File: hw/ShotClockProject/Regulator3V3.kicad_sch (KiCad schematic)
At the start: 11 parts, among them U2 TPS63000

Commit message: Finished rough layout of PCB (ready for review)
Changed battery polarity to match the batteries I have.
Added power led to voltage regulator
Removed old comments from schematic
Gave all footprints a 3D model
Replaced batttery footprint with a SMD JST 3 pins horizontal connector
Finished rough placement of components
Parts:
- added D2: G_LED, LED_SMD:LED_0603_1608Metric, symbol Device:LED
- added R10: 1k5, Resistor_SMD:R_0402_1005Metric, symbol Device:R
- U2: footprint Package_SON:Texas_DRC0010J_ThermalVias -> Package_SON_Altered:Texas_DRC0010J_ThermalVias_Altered
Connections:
- net 3v3_out: now also D2.1 (K), R10.1; no longer C16.1, C17.1, C18.1, R11.1, U2.1 (VOUT)
- net GND: now also R10.2
- new net: C16.1, C17.1, C18.1, D2.2 (A), R11.1, U2.1 (VOUT)
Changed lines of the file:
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@@
   (junction (at 83.82 67.31) (diameter 0) (color 0 0 0 0)
   )
+  (junction (at 139.7 38.1) (diameter 0) (color 0 0 0 0)
+  )
   (junction (at 139.7 48.26) (diameter 0) (color 0 0 0 0)
   )
-  (junction (at 139.7 38.1) (diameter 0) (color 0 0 0 0)
-  )
   (junction (at 59.69 38.1) (diameter 0) (color 0 0 0 0)
   )
   (junction (at 68.58 43.18) (diameter 0) (color 0 0 0 0)
   )
+  (junction (at 156.21 38.1) (diameter 0) (color 0 0 0 0)
+  )
   (junction (at 66.04 45.72) (diameter 0) (color 0 0 0 0)
   )
@@
     (stroke (width 0) (type default))
   )
+  (wire (pts (xy 139.7 38.1) (xy 139.7 40.64))
+    (stroke (width 0) (type default))
+  )
   (wire (pts (xy 139.7 48.26) (xy 134.62 48.26))
     (stroke (width 0) (type default))
@@
     (stroke (width 0) (type default))
   )
-  (wire (pts (xy 139.7 38.1) (xy 149.86 38.1))
-    (stroke (width 0) (type default))
-  )
   (wire (pts (xy 76.2 43.18) (xy 68.58 43.18))
     (stroke (width 0) (type default))
@@
     (stroke (width 0) (type default))
   )
+  (wire (pts (xy 154.94 38.1) (xy 156.21 38.1))
+    (stroke (width 0) (type default))
+  )
   (wire (pts (xy 102.87 45.72) (xy 96.52 45.72))
     (stroke (width 0) (type default))
@@
     (stroke (width 0) (type default))
   )
-  (wire (pts (xy 139.7 38.1) (xy 113.03 38.1))
+  (wire (pts (xy 156.21 38.1) (xy 156.21 43.18))
+    (stroke (width 0) (type default))
+  )
+  (wire (pts (xy 113.03 38.1) (xy 139.7 38.1))
     (stroke (width 0) (type default))
   )
@@
     (stroke (width 0) (type default))
   )
+  (wire (pts (xy 139.7 38.1) (xy 147.32 38.1))
+    (stroke (width 0) (type default))
+  )
   (wire (pts (xy 59.69 38.1) (xy 53.34 38.1))
     (stroke (width 0) (type default))
@@
     (stroke (width 0) (type default))
   )
+  (wire (pts (xy 156.21 50.8) (xy 156.21 53.34))
+    (stroke (width 0) (type default))
+  )
   (wire (pts (xy 73.66 48.26) (xy 73.66 49.53))
     (stroke (width 0) (type default))
@@
     (stroke (width 0) (type default))
   )
-  (wire (pts (xy 139.7 38.1) (xy 139.7 40.64))
+  (wire (pts (xy 156.21 38.1) (xy 157.48 38.1))
     (stroke (width 0) (type default))
   )
@@
     (effects (font (size 2.5 2.5) (color 255 0 0 1)) (justify left bottom))
   )
-  (hierarchical_label "3v3_out" (shape output) (at 149.86 38.1 0) (fields_autoplaced)
+  (hierarchical_label "3v3_out" (shape output) (at 157.48 38.1 0) (fields_autoplaced)
     (effects (font (size 1.27 1.27)) (justify left))
   )
   (hierarchical_label "batt_in" (shape input) (at 31.75 38.1 180) (fields_autoplaced)
     (effects (font (size 1.27 1.27)) (justify right))
+  )
+  (symbol (lib_id "Device:R") (at 156.21 46.99 0) (mirror y) (unit 1)
+    (in_bom yes) (on_board yes) (dnp no)
+    (property "Reference" "R10" (at 158.75 45.72 0)
+      (effects (font (size 1.27 1.27)) (justify right))
+    )
+    (property "Value" "1k5" (at 158.75 48.26 0)
+      (effects (font (size 1.27 1.27)) (justify right))
+    )
+    (property "Footprint" "Resistor_SMD:R_0402_1005Metric" (at 157.988 46.99 90)
+      (effects (font (size 1.27 1.27)) hide)
+    )
+    (property "Datasheet" "~" (at 156.21 46.99 0)
+      (effects (font (size 1.27 1.27)) hide)
+    )
+    (pin "1")
+    (pin "2")
+    (instances
+      (project "ShotClockProject"
+        (path "/5fd859aa-754d-49c2-9762-3f7ebe3bb64c"
+          (reference "R10") (unit 1)
+        )
+        (path "/5fd859aa-754d-49c2-9762-3f7ebe3bb64c/17367eb9-0f4d-4017-b1ca-d50430410a5d"
+          (reference "R28") (unit 1)
+        )
+      )
+    )
+  )
+  (symbol (lib_id "power:GND") (at 156.21 53.34 0) (mirror y) (unit 1)
+    (in_bom yes) (on_board yes) (dnp no) (fields_autoplaced)
+    (property "Reference" "#PWR033" (at 156.21 59.69 0)
+      (effects (font (size 1.27 1.27)) hide)
+    )
+    (property "Value" "GND" (at 156.21 58.42 0)
+      (effects (font (size 1.27 1.27)) hide)
+    )
+    (property "Footprint" "" (at 156.21 53.34 0)
+      (effects (font (size 1.27 1.27)) hide)
+    )
+    (property "Datasheet" "" (at 156.21 53.34 0)
+      (effects (font (size 1.27 1.27)) hide)
+    )
+    (pin "1")
+    (instances
+      (project "ShotClockProject"
+        (path "/5fd859aa-754d-49c2-9762-3f7ebe3bb64c"
+          (reference "#PWR033") (unit 1)
+        )
+        (path "/5fd859aa-754d-49c2-9762-3f7ebe3bb64c/17367eb9-0f4d-4017-b1ca-d50430410a5d"
+          (reference "#PWR074") (unit 1)
+        )
+      )
+    )
   )
   (symbol (lib_id "Device:C") (at 144.78 44.45 0) (mirror y) (unit 1)
@@
       (effects (font (size 1.27 1.27)))
     )
-    (property "Footprint" "Package_SON:Texas_DRC0010J_ThermalVias" (at 107.95 62.23 0)
+    (property "Footprint" "Package_SON_Altered:Texas_DRC0010J_ThermalVias_Altered" (at 107.95 62.23 0)
       (effects (font (size 1.27 1.27)) hide)
     )
@@
         )
       )
+    )
+  )
+  (symbol (lib_id "Device:LED") (at 151.13 38.1 0) (mirror y) (unit 1)
+    (in_bom yes) (on_board yes) (dnp no)
+    (property "Reference" "D2" (at 152.4 33.02 0)
+      (effects (font (size 1.27 1.27)) (justify right))
+    )
+    (property "Value" "G_LED" (at 149.86 35.56 0)
+      (effects (font (size 1.27 1.27)) (justify right))
+    )
+    (property "Footprint" "LED_SMD:LED_0603_1608Metric" (at 151.13 38.1 0)
+      (effects (font (size 1.27 1.27)) hide)
+    )
+    (property "Datasheet" "~" (at 151.13 38.1 0)
+      (effects (font (size 1.27 1.27)) hide)
+    )
+    (pin "1")
+    (pin "2")
+    (instances
+      (project "ShotClockProject"
+        (path "/5fd859aa-754d-49c2-9762-3f7ebe3bb64c"
+          (reference "D2") (unit 1)
+        )
+        (path "/5fd859aa-754d-49c2-9762-3f7ebe3bb64c/d287d155-1951-4d4f-8d6c-570f03bc79f5"
+          (reference "D3") (unit 1)
+        )
+        (path "/5fd859aa-754d-49c2-9762-3f7ebe3bb64c/17367eb9-0f4d-4017-b1ca-d50430410a5d"
+          (reference "D5") (unit 1)
+        )
+      )

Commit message: First feedback round from Luc on schematic
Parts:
- L1: value L -> 2.2uH
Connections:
- net 3v3_out: now also C16.1, C17.1, C18.1, D2.2 (A), R11.1, U2.1 (VOUT); no longer D2.1 (K), R10.1
- new net: D2.1 (K), R10.1
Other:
- moved on the sheet: D2, R10
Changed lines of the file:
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@@
   (junction (at 83.82 67.31) (diameter 0) (color 0 0 0 0)
   )
+  (junction (at 154.94 38.1) (diameter 0) (color 0 0 0 0)
+  )
   (junction (at 139.7 38.1) (diameter 0) (color 0 0 0 0)
   )
@@
   (junction (at 68.58 43.18) (diameter 0) (color 0 0 0 0)
   )
-  (junction (at 156.21 38.1) (diameter 0) (color 0 0 0 0)
-  )
   (junction (at 66.04 45.72) (diameter 0) (color 0 0 0 0)
   )
@@
     (stroke (width 0) (type default))
   )
-  (wire (pts (xy 154.94 38.1) (xy 156.21 38.1))
+  (wire (pts (xy 154.94 38.1) (xy 154.94 41.91))
     (stroke (width 0) (type default))
   )
@@
     (stroke (width 0) (type default))
   )
+  (wire (pts (xy 154.94 49.53) (xy 154.94 50.8))
+    (stroke (width 0) (type default))
+  )
   (wire (pts (xy 78.74 67.31) (xy 83.82 67.31))
     (stroke (width 0) (type default))
@@
     (stroke (width 0) (type default))
   )
-  (wire (pts (xy 156.21 38.1) (xy 156.21 43.18))
+  (wire (pts (xy 154.94 38.1) (xy 172.72 38.1))
     (stroke (width 0) (type default))
   )
@@
     (stroke (width 0) (type default))
   )
-  (wire (pts (xy 139.7 38.1) (xy 147.32 38.1))
+  (wire (pts (xy 139.7 38.1) (xy 154.94 38.1))
     (stroke (width 0) (type default))
   )
@@
     (stroke (width 0) (type default))
   )
-  (wire (pts (xy 156.21 50.8) (xy 156.21 53.34))
-    (stroke (width 0) (type default))
-  )
   (wire (pts (xy 73.66 48.26) (xy 73.66 49.53))
     (stroke (width 0) (type default))
@@
     (stroke (width 0) (type default))
   )
-  (wire (pts (xy 156.21 38.1) (xy 157.48 38.1))
-    (stroke (width 0) (type default))
-  )
   (wire (pts (xy 73.66 58.42) (xy 73.66 57.15))
     (stroke (width 0) (type default))
   )
   (wire (pts (xy 31.75 38.1) (xy 41.91 38.1))
+    (stroke (width 0) (type default))
+  )
+  (wire (pts (xy 154.94 58.42) (xy 154.94 60.96))
     (stroke (width 0) (type default))
   )
@@
     (fill (type none))
   )
-  (rectangle (start 19.05 21.59) (end 166.37 91.44)
+  (rectangle (start 19.05 21.59) (end 187.96 91.44)
     (stroke (width 0) (type dash) (color 255 0 0 1))
     (fill (type none))
@@
     (effects (font (size 2.5 2.5) (color 255 0 0 1)) (justify left bottom))
   )
-  (hierarchical_label "3v3_out" (shape output) (at 157.48 38.1 0) (fields_autoplaced)
+  (hierarchical_label "3v3_out" (shape output) (at 172.72 38.1 0) (fields_autoplaced)
     (effects (font (size 1.27 1.27)) (justify left))
   )
@@
     (effects (font (size 1.27 1.27)) (justify right))
   )
-  (symbol (lib_id "Device:R") (at 156.21 46.99 0) (mirror y) (unit 1)
+  (symbol (lib_id "Device:R") (at 154.94 54.61 0) (mirror y) (unit 1)
     (in_bom yes) (on_board yes) (dnp no)
-    (property "Reference" "R10" (at 158.75 45.72 0)
+    (property "Reference" "R10" (at 157.48 53.34 0)
       (effects (font (size 1.27 1.27)) (justify right))
     )
-    (property "Value" "1k5" (at 158.75 48.26 0)
+    (property "Value" "1k5" (at 157.48 55.88 0)
       (effects (font (size 1.27 1.27)) (justify right))
     )
-    (property "Footprint" "Resistor_SMD:R_0402_1005Metric" (at 157.988 46.99 90)
-      (effects (font (size 1.27 1.27)) hide)
-    )
-    (property "Datasheet" "~" (at 156.21 46.99 0)
+    (property "Footprint" "Resistor_SMD:R_0402_1005Metric" (at 156.718 54.61 90)
+      (effects (font (size 1.27 1.27)) hide)
+    )
+    (property "Datasheet" "~" (at 154.94 54.61 0)
       (effects (font (size 1.27 1.27)) hide)
     )
@@
     )
   )
-  (symbol (lib_id "power:GND") (at 156.21 53.34 0) (mirror y) (unit 1)
+  (symbol (lib_id "power:GND") (at 154.94 60.96 0) (mirror y) (unit 1)
     (in_bom yes) (on_board yes) (dnp no) (fields_autoplaced)
-    (property "Reference" "#PWR033" (at 156.21 59.69 0)
-      (effects (font (size 1.27 1.27)) hide)
-    )
-    (property "Value" "GND" (at 156.21 58.42 0)
-      (effects (font (size 1.27 1.27)) hide)
-    )
-    (property "Footprint" "" (at 156.21 53.34 0)
-      (effects (font (size 1.27 1.27)) hide)
-    )
-    (property "Datasheet" "" (at 156.21 53.34 0)
+    (property "Reference" "#PWR033" (at 154.94 67.31 0)
+      (effects (font (size 1.27 1.27)) hide)
+    )
+    (property "Value" "GND" (at 154.94 66.04 0)
+      (effects (font (size 1.27 1.27)) hide)
+    )
+    (property "Footprint" "" (at 154.94 60.96 0)
+      (effects (font (size 1.27 1.27)) hide)
+    )
+    (property "Datasheet" "" (at 154.94 60.96 0)
       (effects (font (size 1.27 1.27)) hide)
     )
@@
     )
   )
-  (symbol (lib_id "Device:LED") (at 151.13 38.1 0) (mirror y) (unit 1)
+  (symbol (lib_id "Device:LED") (at 154.94 45.72 270) (mirror x) (unit 1)
     (in_bom yes) (on_board yes) (dnp no)
-    (property "Reference" "D2" (at 152.4 33.02 0)
+    (property "Reference" "D2" (at 160.02 46.99 0)
       (effects (font (size 1.27 1.27)) (justify right))
     )
-    (property "Value" "G_LED" (at 149.86 35.56 0)
+    (property "Value" "G_LED" (at 157.48 44.45 0)
       (effects (font (size 1.27 1.27)) (justify right))
     )
-    (property "Footprint" "LED_SMD:LED_0603_1608Metric" (at 151.13 38.1 0)
-      (effects (font (size 1.27 1.27)) hide)
-    )
-    (property "Datasheet" "~" (at 151.13 38.1 0)
+    (property "Footprint" "LED_SMD:LED_0603_1608Metric" (at 154.94 45.72 0)
+      (effects (font (size 1.27 1.27)) hide)
+    )
+    (property "Datasheet" "~" (at 154.94 45.72 0)
       (effects (font (size 1.27 1.27)) hide)
     )
@@
   )
   (symbol (lib_id "Device:L") (at 73.66 53.34 0) (mirror y) (unit 1)
-    (in_bom yes) (on_board yes) (dnp no) (fields_autoplaced)
-    (property "Reference" "L1" (at 72.39 52.07 0)
-      (effects (font (size 1.27 1.27)) (justify left))
-    )
-    (property "Value" "L" (at 72.39 54.61 0)
-      (effects (font (size 1.27 1.27)) (justify left))
+    (in_bom yes) (on_board yes) (dnp no)
+    (property "Reference" "L1" (at 67.31 54.61 0)
+      (effects (font (size 1.27 1.27)) (justify right))
+    )
+    (property "Value" "2.2uH" (at 67.31 57.15 0)
+      (effects (font (size 1.27 1.27)) (justify right))
     )
     (property "Footprint" "Inductor_SMD:L_Sunlord_SWPA3012S" (at 73.66 53.34 0)

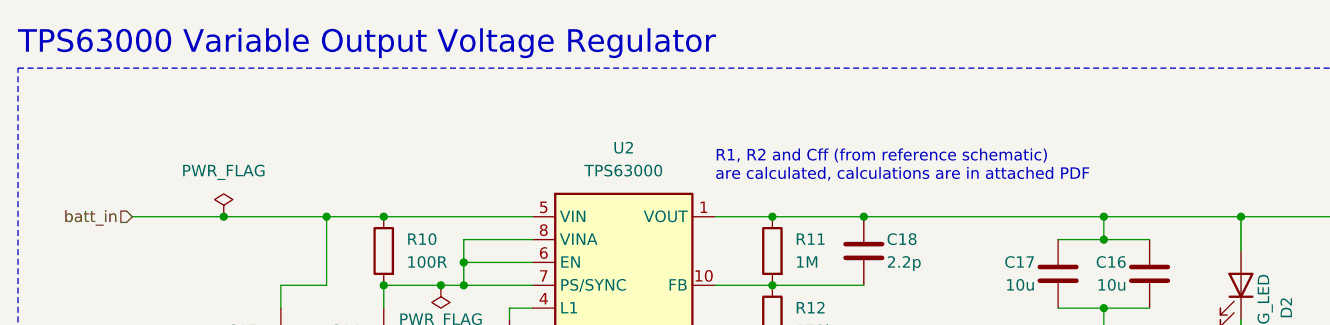
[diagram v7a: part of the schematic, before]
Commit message: Started on second PCB, and added 5V regulator
5V regulator added to main pcb for the segment displays, using same TPS63000 chip, but with a different selector resistor to choose for 5V

Added second project to contain the display PCBA design.

Calculated the current usage of the displays with different current limiting resistors on the LEDs.

Calculated the  current limit resistors for transistors behind LEDs
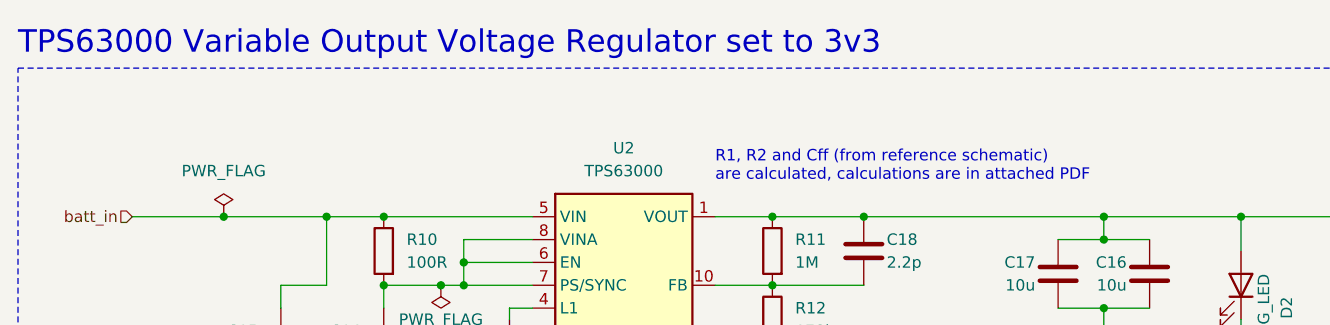
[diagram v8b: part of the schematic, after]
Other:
- note added: "TPS63000 Variable Output Voltage Regulator set to 3v3"
- note removed: "TPS63000 Variable Output Voltage Regulator"
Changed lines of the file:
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@@
     (effects (font (size 1.27 1.27)) (justify left bottom))
   )
-  (text "TPS63000 Variable Output Voltage Regulator" (at 19.05 20.32 0)
+  (text "TPS63000 Variable Output Voltage Regulator set to 3v3"
+    (at 19.05 20.32 0)
     (effects (font (size 2.5 2.5) (color 255 0 0 1)) (justify left bottom))
   )
@@
           (reference "R28") (unit 1)
         )
+        (path "/5fd859aa-754d-49c2-9762-3f7ebe3bb64c/83d8d19c-1376-4688-800d-ae057ad1fe11"
+          (reference "R38") (unit 1)
+        )
       )
     )
@@
           (reference "#PWR074") (unit 1)
         )
+        (path "/5fd859aa-754d-49c2-9762-3f7ebe3bb64c/83d8d19c-1376-4688-800d-ae057ad1fe11"
+          (reference "#PWR088") (unit 1)
+        )
       )
     )
@@
           (reference "C19") (unit 1)
         )
+        (path "/5fd859aa-754d-49c2-9762-3f7ebe3bb64c/83d8d19c-1376-4688-800d-ae057ad1fe11"
+          (reference "C31") (unit 1)
+        )
       )
     )
@@
         (path "/5fd859aa-754d-49c2-9762-3f7ebe3bb64c/17367eb9-0f4d-4017-b1ca-d50430410a5d"
           (reference "#PWR046") (unit 1)
+        )
+        (path "/5fd859aa-754d-49c2-9762-3f7ebe3bb64c/83d8d19c-1376-4688-800d-ae057ad1fe11"
+          (reference "#PWR085") (unit 1)
         )
       )
@@
           (reference "#FLG09") (unit 1)
         )
+        (path "/5fd859aa-754d-49c2-9762-3f7ebe3bb64c/83d8d19c-1376-4688-800d-ae057ad1fe11"
+          (reference "#FLG012") (unit 1)
+        )
       )
     )
@@
           (reference "C21") (unit 1)
         )
+        (path "/5fd859aa-754d-49c2-9762-3f7ebe3bb64c/83d8d19c-1376-4688-800d-ae057ad1fe11"
+          (reference "C28") (unit 1)
+        )
       )
     )
@@
           (reference "R20") (unit 1)
         )
+        (path "/5fd859aa-754d-49c2-9762-3f7ebe3bb64c/83d8d19c-1376-4688-800d-ae057ad1fe11"
+          (reference "R35") (unit 1)
+        )
       )
     )
@@
         (path "/5fd859aa-754d-49c2-9762-3f7ebe3bb64c/17367eb9-0f4d-4017-b1ca-d50430410a5d"
           (reference "C20") (unit 1)
+        )
+        (path "/5fd859aa-754d-49c2-9762-3f7ebe3bb64c/83d8d19c-1376-4688-800d-ae057ad1fe11"
+          (reference "C27") (unit 1)
         )
       )
@@
           (reference "U3") (unit 1)
         )
+        (path "/5fd859aa-754d-49c2-9762-3f7ebe3bb64c/83d8d19c-1376-4688-800d-ae057ad1fe11"
+          (reference "U5") (unit 1)
+        )
       )
     )
@@
           (reference "#PWR050") (unit 1)
         )
+        (path "/5fd859aa-754d-49c2-9762-3f7ebe3bb64c/83d8d19c-1376-4688-800d-ae057ad1fe11"
+          (reference "#PWR072") (unit 1)
+        )
       )
     )
@@
         (path "/5fd859aa-754d-49c2-9762-3f7ebe3bb64c/17367eb9-0f4d-4017-b1ca-d50430410a5d"
           (reference "#PWR045") (unit 1)
+        )
+        (path "/5fd859aa-754d-49c2-9762-3f7ebe3bb64c/83d8d19c-1376-4688-800d-ae057ad1fe11"
+          (reference "#PWR086") (unit 1)
         )
       )
@@
           (reference "D5") (unit 1)
         )
+        (path "/5fd859aa-754d-49c2-9762-3f7ebe3bb64c/83d8d19c-1376-4688-800d-ae057ad1fe11"
+          (reference "D7") (unit 1)
+        )
       )
     )
@@
         (path "/5fd859aa-754d-49c2-9762-3f7ebe3bb64c/17367eb9-0f4d-4017-b1ca-d50430410a5d"
           (reference "#PWR048") (unit 1)
+        )
+        (path "/5fd859aa-754d-49c2-9762-3f7ebe3bb64c/83d8d19c-1376-4688-800d-ae057ad1fe11"
+          (reference "#PWR070") (unit 1)
         )
       )
@@
           (reference "#FLG07") (unit 1)
         )
+        (path "/5fd859aa-754d-49c2-9762-3f7ebe3bb64c/83d8d19c-1376-4688-800d-ae057ad1fe11"
+          (reference "#FLG010") (unit 1)
+        )
       )
     )
@@
           (reference "C18") (unit 1)
         )
+        (path "/5fd859aa-754d-49c2-9762-3f7ebe3bb64c/83d8d19c-1376-4688-800d-ae057ad1fe11"
+          (reference "C30") (unit 1)
+        )
       )
     )
@@
           (reference "#PWR051") (unit 1)
         )
+        (path "/5fd859aa-754d-49c2-9762-3f7ebe3bb64c/83d8d19c-1376-4688-800d-ae057ad1fe11"
+          (reference "#PWR071") (unit 1)
+        )
       )
     )
@@
           (reference "R21") (unit 1)
         )
+        (path "/5fd859aa-754d-49c2-9762-3f7ebe3bb64c/83d8d19c-1376-4688-800d-ae057ad1fe11"
+          (reference "R37") (unit 1)
+        )
       )
     )
@@
         (path "/5fd859aa-754d-49c2-9762-3f7ebe3bb64c/17367eb9-0f4d-4017-b1ca-d50430410a5d"
           (reference "#PWR049") (unit 1)
+        )
+        (path "/5fd859aa-754d-49c2-9762-3f7ebe3bb64c/83d8d19c-1376-4688-800d-ae057ad1fe11"
+          (reference "#PWR082") (unit 1)
         )
       )
@@
           (reference "NT2") (unit 1)
         )
+        (path "/5fd859aa-754d-49c2-9762-3f7ebe3bb64c/83d8d19c-1376-4688-800d-ae057ad1fe11"
+          (reference "NT3") (unit 1)
+        )
       )
     )
@@
           (reference "C17") (unit 1)
         )
+        (path "/5fd859aa-754d-49c2-9762-3f7ebe3bb64c/83d8d19c-1376-4688-800d-ae057ad1fe11"
+          (reference "C29") (unit 1)
+        )
       )
     )
@@
           (reference "R19") (unit 1)
         )
+        (path "/5fd859aa-754d-49c2-9762-3f7ebe3bb64c/83d8d19c-1376-4688-800d-ae057ad1fe11"
+          (reference "R24") (unit 1)
+        )
       )
     )
@@
           (reference "#PWR047") (unit 1)
         )
+        (path "/5fd859aa-754d-49c2-9762-3f7ebe3bb64c/83d8d19c-1376-4688-800d-ae057ad1fe11"
+          (reference "#PWR069") (unit 1)
+        )
       )
     )
@@
         (path "/5fd859aa-754d-49c2-9762-3f7ebe3bb64c/17367eb9-0f4d-4017-b1ca-d50430410a5d"
           (reference "L1") (unit 1)
+        )
+        (path "/5fd859aa-754d-49c2-9762-3f7ebe3bb64c/83d8d19c-1376-4688-800d-ae057ad1fe11"
+          (reference "L2") (unit 1)
         )
       )
@@
           (reference "#FLG08") (unit 1)
         )
-      )
+        (path "/5fd859aa-754d-49c2-9762-3f7ebe3bb64c/83d8d19c-1376-4688-800d-ae057ad1fe11"
+          (reference "#FLG011") (unit 1)
+        )
+      )
